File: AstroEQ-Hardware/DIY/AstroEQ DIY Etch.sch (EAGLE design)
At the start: 56 parts, among them IC1 ATMEGA162-16PU, IC2 PIC18F14K50-I/P, IC3 78L05, J1 POWER_JACKPTH, M1 Motor Driver, M2 Motor Driver, Q1 BS270, X1 16MHz, X2 12MHz

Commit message: Update DIY Etch Schematic Formatting (no actual design changes)
Tidy up the schematic and add frame to match the PTH V4.6 tidy up
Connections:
- net MISO renamed IO3-MISO
- net MOSI renamed ESTOP-MOSI
- net SCLK renamed STAT-SCLK
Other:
- moved on the sheet: C1, C10, C11, C12, C13, C14, C15, C2, C3, C4, C5, C6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

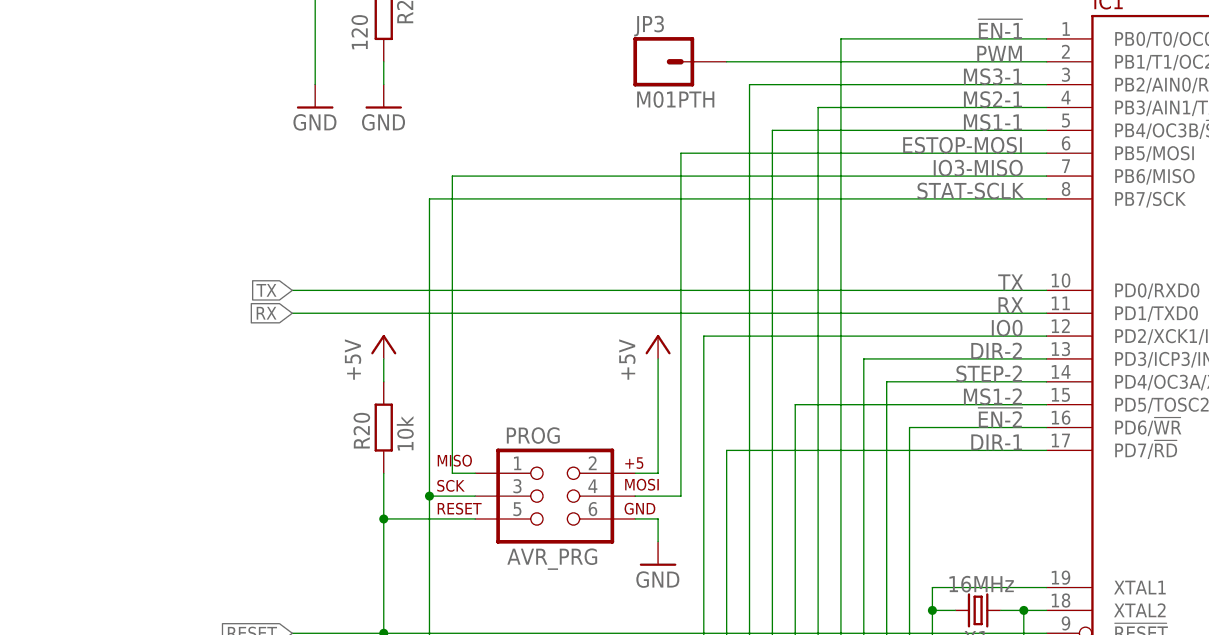
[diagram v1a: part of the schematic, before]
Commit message: Add extra target speed resistor to AstroEQ DIY
Bump version to hardware V4.8
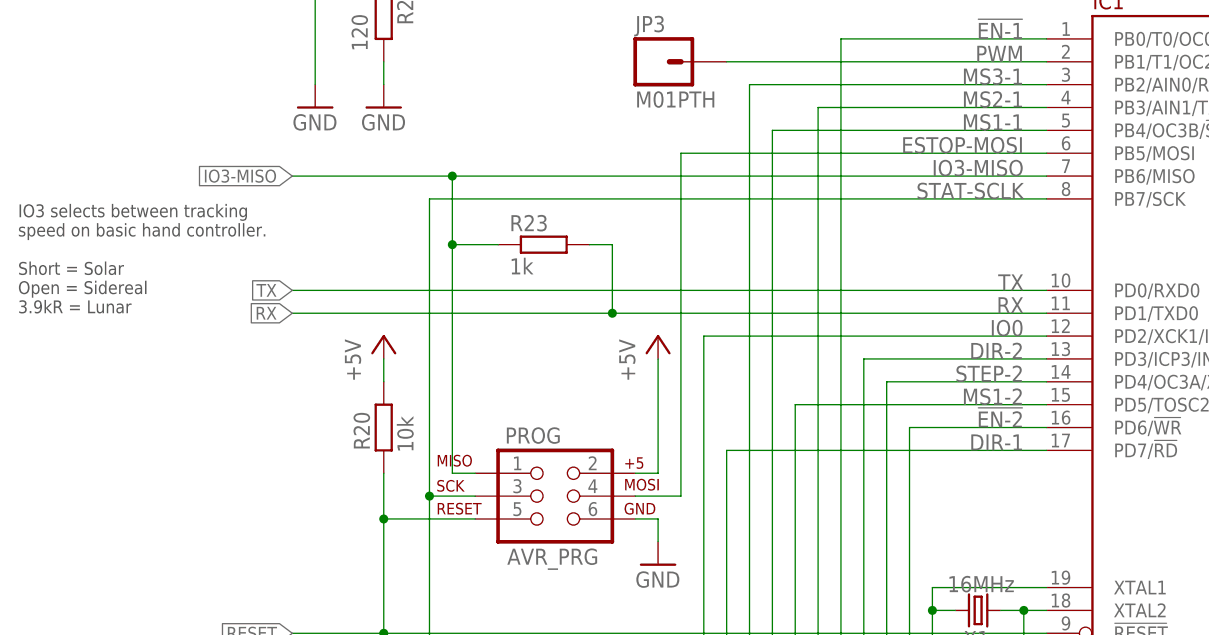
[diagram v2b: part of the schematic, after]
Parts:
- added R23: 1k, rcl:R-EU_0204/7
- SJ1: device jumper:JP2E -> jumper:JP2EL
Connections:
- net IO3-MISO: now also R23.1
- net RX: now also R23.2
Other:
- note added: "IO3 selects between tracking speed on basic hand controller. Short = Solar Open = Sidereal 3.9kR = Lunar"
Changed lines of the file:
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@@
 <attribute name="OC_FARNELL" value="9342400"/>
 </part>
-<part name="SJ1" library="jumper" deviceset="JP2E" device="">
+<part name="SJ1" library="jumper" deviceset="JP2E" device="L">
 <attribute name="MF" value=""/>
 <attribute name="MPN" value=""/>
@@
 </part>
 <part name="GND11" library="supply1" deviceset="GND" device=""/>
+<part name="R23" library="rcl" deviceset="R-EU_" device="0204/7" value="1k">
+<attribute name="MF" value="MULTICOMP"/>
+<attribute name="MPN" value="MF12 1K"/>
+<attribute name="OC_FARNELL" value="9342400"/>
+</part>
 </parts>
 <sheets>
@@
 <description>AstroEQ</description>
 <plain>
+<text x="20.32" y="91.44" size="1.4224" layer="97">IO3 selects between tracking
+speed on basic hand controller.
+Short = Solar
+Open = Sidereal
+3.9kR = Lunar</text>
 </plain>
 <instances>
@@
 <instance part="GND7" gate="1" x="165.1" y="162.56"/>
 <instance part="GND11" gate="1" x="66.04" y="25.4"/>
+<instance part="R23" gate="G$1" x="78.74" y="99.06">
+<attribute name="OC_FARNELL" value="9342400" x="78.74" y="99.06" size="1.778" layer="96" rot="R90" display="off"/>
+<attribute name="MF" value="MULTICOMP" x="78.74" y="99.06" size="1.778" layer="96" rot="R90" display="off"/>
+<attribute name="MPN" value="MF12 1K" x="78.74" y="99.06" size="1.778" layer="96" rot="R90" display="off"/>
+</instance>
 </instances>
 <busses>
@@
 <segment>
 <pinref part="IC1" gate="G$1" pin="PD1/TXD0"/>
-<wire x1="134.62" y1="91.44" x2="50.8" y2="91.44" width="0.1524" layer="91"/>
+<wire x1="134.62" y1="91.44" x2="86.36" y2="91.44" width="0.1524" layer="91"/>
 <label x="132.08" y="91.44" size="1.778" layer="95" rot="MR0"/>
 <label x="50.8" y="91.44" size="1.4224" layer="95" font="vector" ratio="10" rot="R180" xref="yes"/>
+<wire x1="86.36" y1="91.44" x2="50.8" y2="91.44" width="0.1524" layer="91"/>
+<wire x1="83.82" y1="99.06" x2="86.36" y2="99.06" width="0.1524" layer="91"/>
+<wire x1="86.36" y1="99.06" x2="86.36" y2="91.44" width="0.1524" layer="91"/>
+<junction x="86.36" y="91.44"/>
+<pinref part="R23" gate="G$1" pin="2"/>
 </segment>
 <segment>
@@
 <pinref part="PROG" gate="G$1" pin="1"/>
 <wire x1="71.12" y1="73.66" x2="68.58" y2="73.66" width="0.1524" layer="91"/>
-<wire x1="68.58" y1="73.66" x2="68.58" y2="106.68" width="0.1524" layer="91"/>
+<wire x1="68.58" y1="73.66" x2="68.58" y2="99.06" width="0.1524" layer="91"/>
+<wire x1="68.58" y1="99.06" x2="68.58" y2="106.68" width="0.1524" layer="91"/>
 <wire x1="68.58" y1="106.68" x2="134.62" y2="106.68" width="0.1524" layer="91"/>
 <label x="132.08" y="106.68" size="1.778" layer="95" rot="MR0"/>
+<wire x1="73.66" y1="99.06" x2="68.58" y2="99.06" width="0.1524" layer="91"/>
+<wire x1="68.58" y1="106.68" x2="50.8" y2="106.68" width="0.1524" layer="91"/>
+<label x="50.8" y="106.68" size="1.4224" layer="95" font="vector" ratio="10" rot="R180" xref="yes"/>
+<junction x="68.58" y="106.68"/>
+<junction x="68.58" y="99.06"/>
+<pinref part="R23" gate="G$1" pin="1"/>
 </segment>
 </net>
@@
 </schematic>
 </drawing>
+<compatibility>
+<note version="6.3" minversion="6.2.2" severity="warning">
+Since Version 6.2.2 text objects can contain more than one line,
+which will not be processed correctly with this version.
+</note>
+</compatibility>
 </eagle>
